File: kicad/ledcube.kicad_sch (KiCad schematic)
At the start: 46 parts, among them J1 Conn_01x04, P1 USB_C_Plug_USB2.0

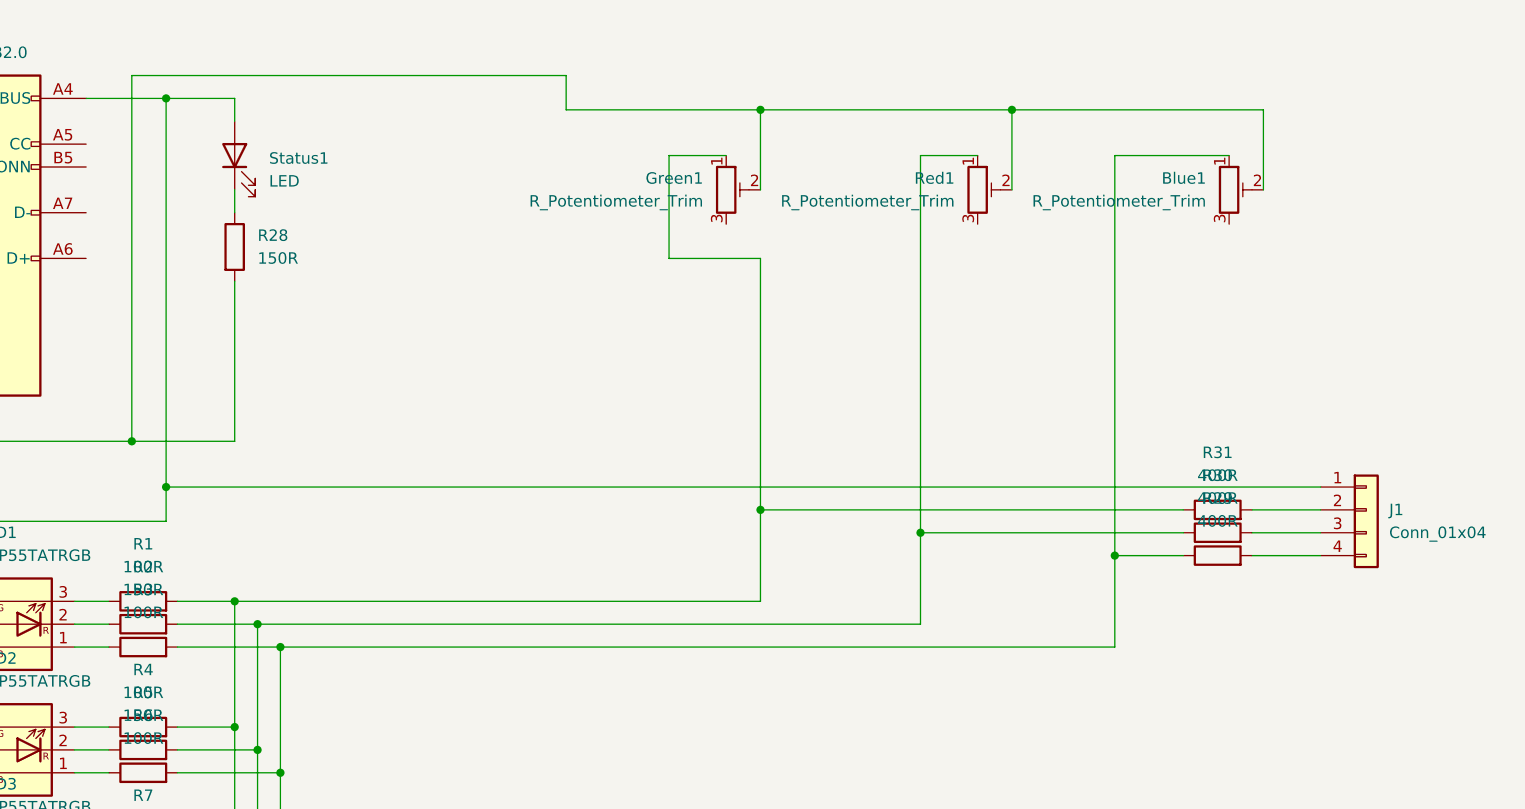
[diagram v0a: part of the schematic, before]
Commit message: Revert "Added 12V support for Motherboards"
This reverts commit cbf7dcde6a27399269292319d1f5b2d3f34ebe3c.
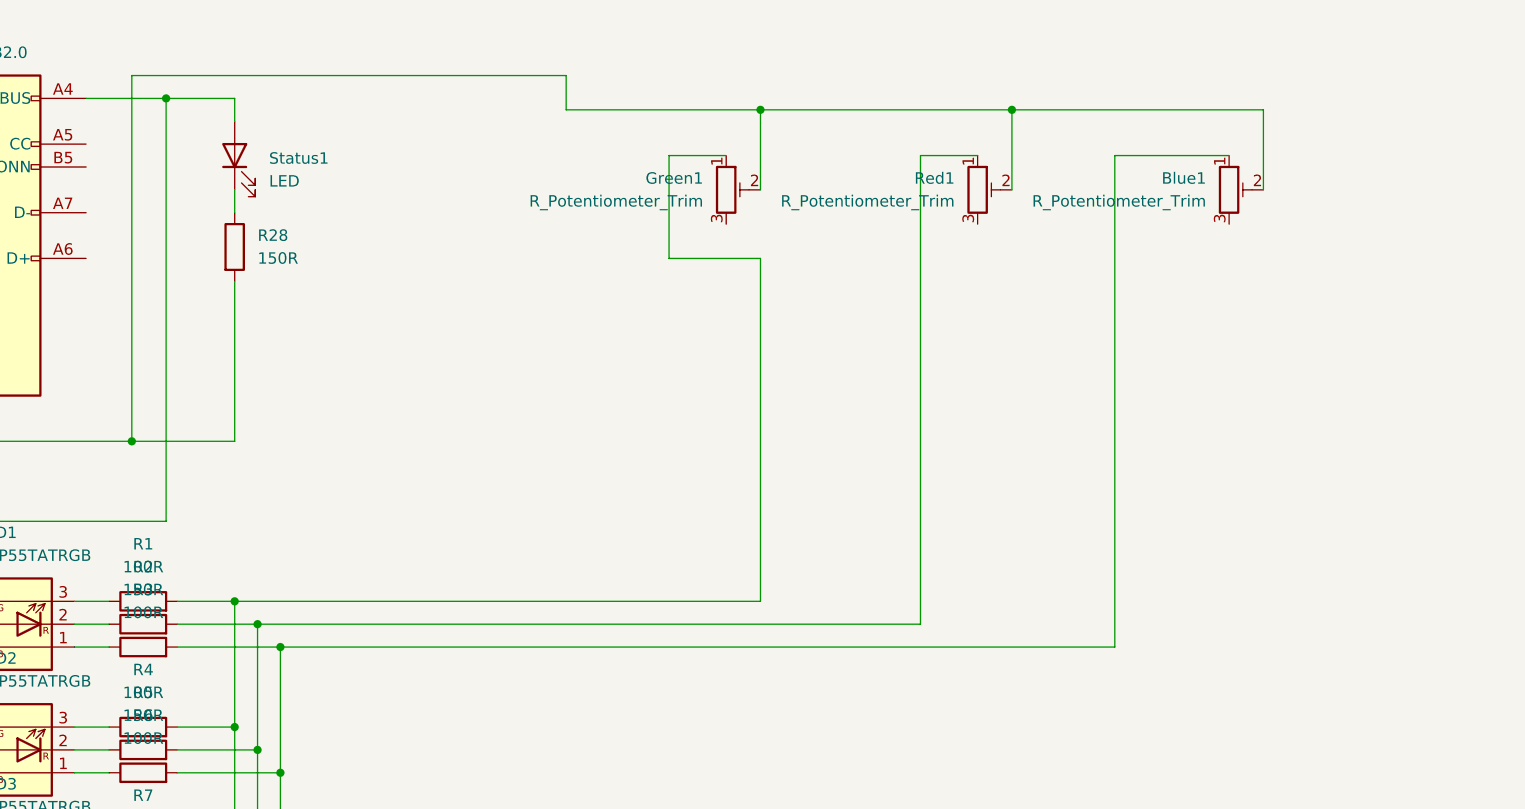
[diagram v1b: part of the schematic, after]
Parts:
- removed J1: Conn_01x04, symbol Connector_Generic:Conn_01x04
- removed R29, R30, R31: 400R, Resistor_SMD:R_0603_1608Metric, symbol Device:R

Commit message: Added 12V support for Motherboards
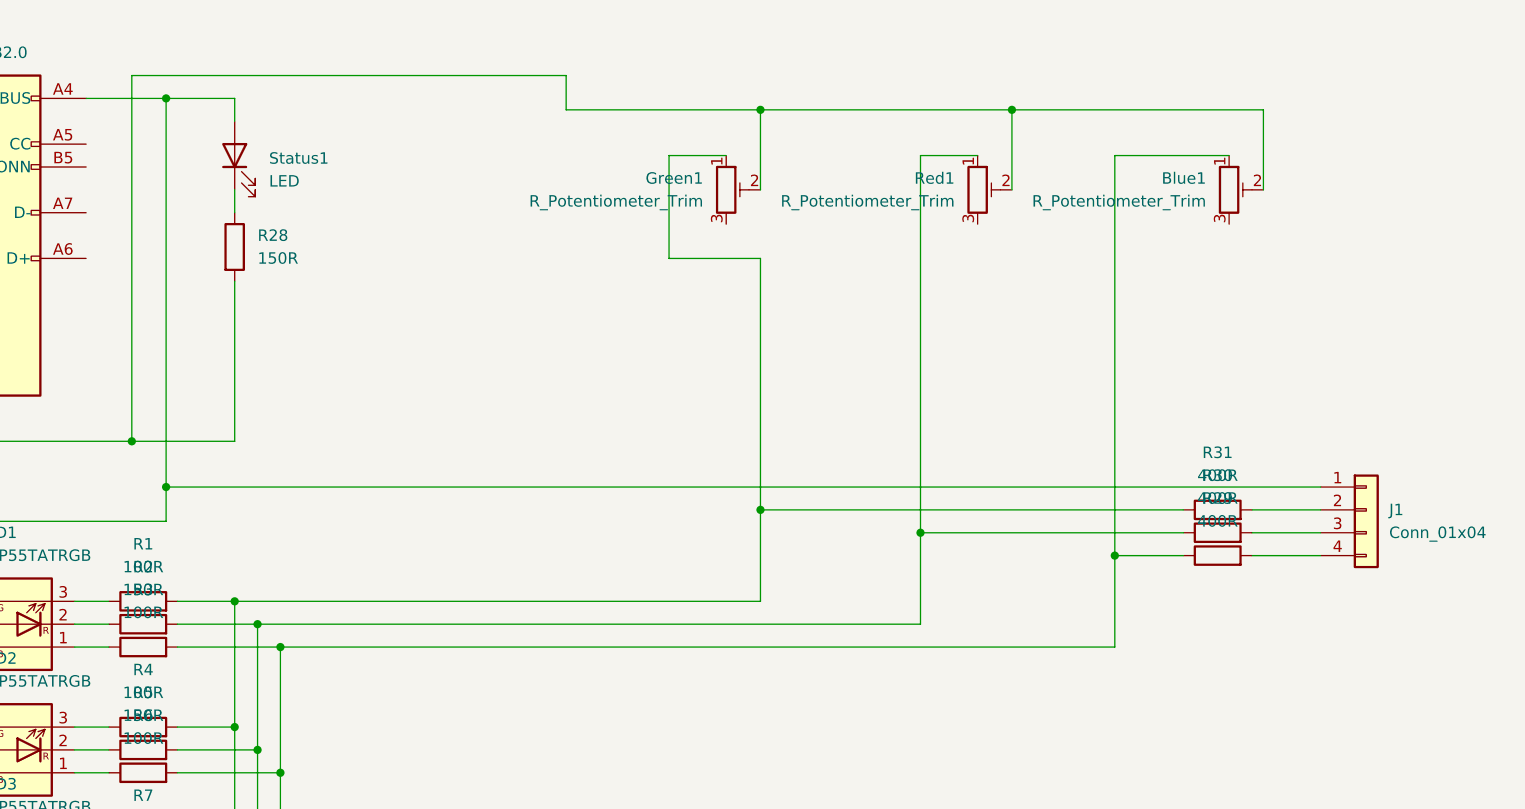
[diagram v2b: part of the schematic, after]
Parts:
- added J1: Conn_01x04, symbol Connector_Generic:Conn_01x04
- added R29, R30, R31: 400R, Resistor_SMD:R_0603_1608Metric, symbol Device:R
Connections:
- net at Blue1.1, R12.2, R15.2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: now also R29.1
- net at Green1.1, R1.2, R10.2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: now also R31.1
- net at D1.4 (AG), D1.5 (AR), D1.6 (AB)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: now also J1.1 (Pin_1)
- net at R11.2, R14.2, R17.2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: now also R30.1
- new net: J1.4 (Pin_4), R29.2
- new net: J1.3 (Pin_3), R30.2
- new net: J1.2 (Pin_2), R31.2
